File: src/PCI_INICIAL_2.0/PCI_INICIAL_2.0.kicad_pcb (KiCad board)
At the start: 2 copper layers, 60 x 50.8 mm, 9 parts, among them J1 2 male pin header, SW1 Switch, U1 ESP32, U2 MPU9250 Module, U3 TP4056

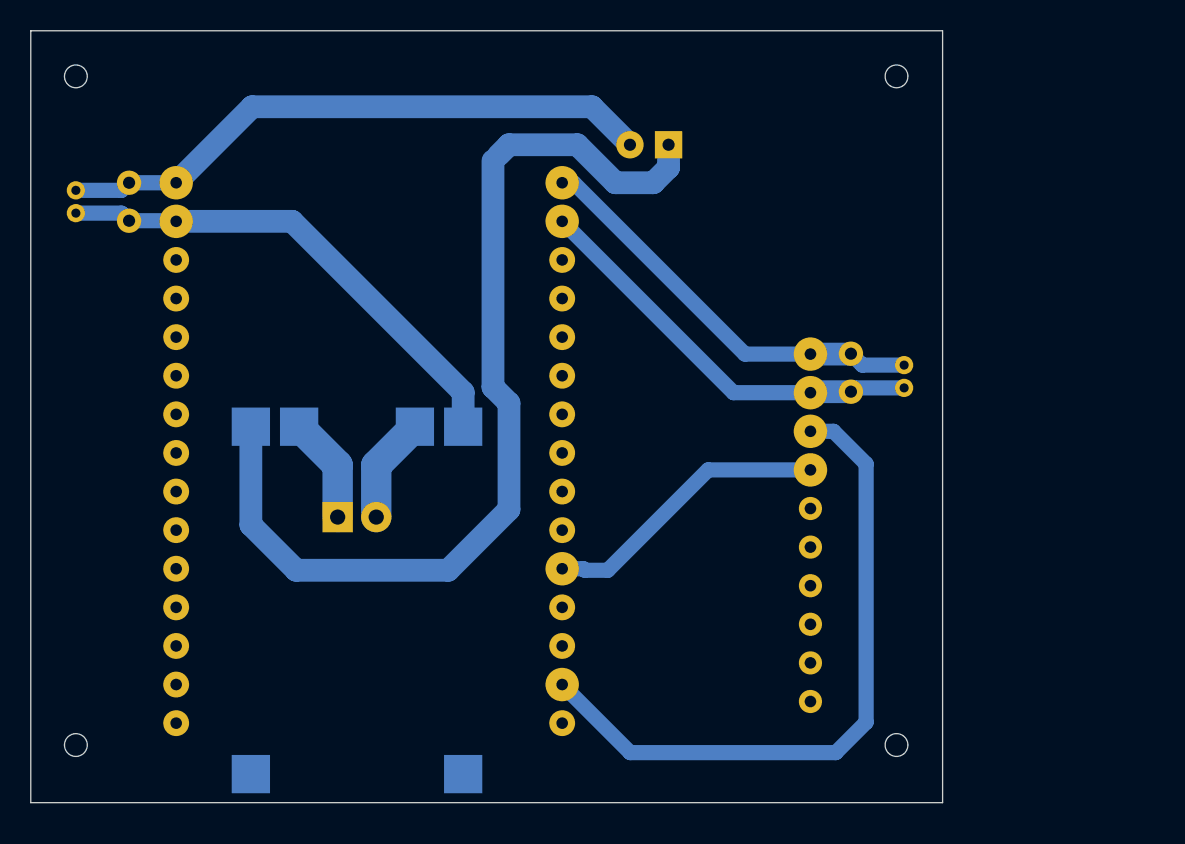
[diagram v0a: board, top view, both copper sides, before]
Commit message: feat: adiciona arquivos 2.0 de PCI
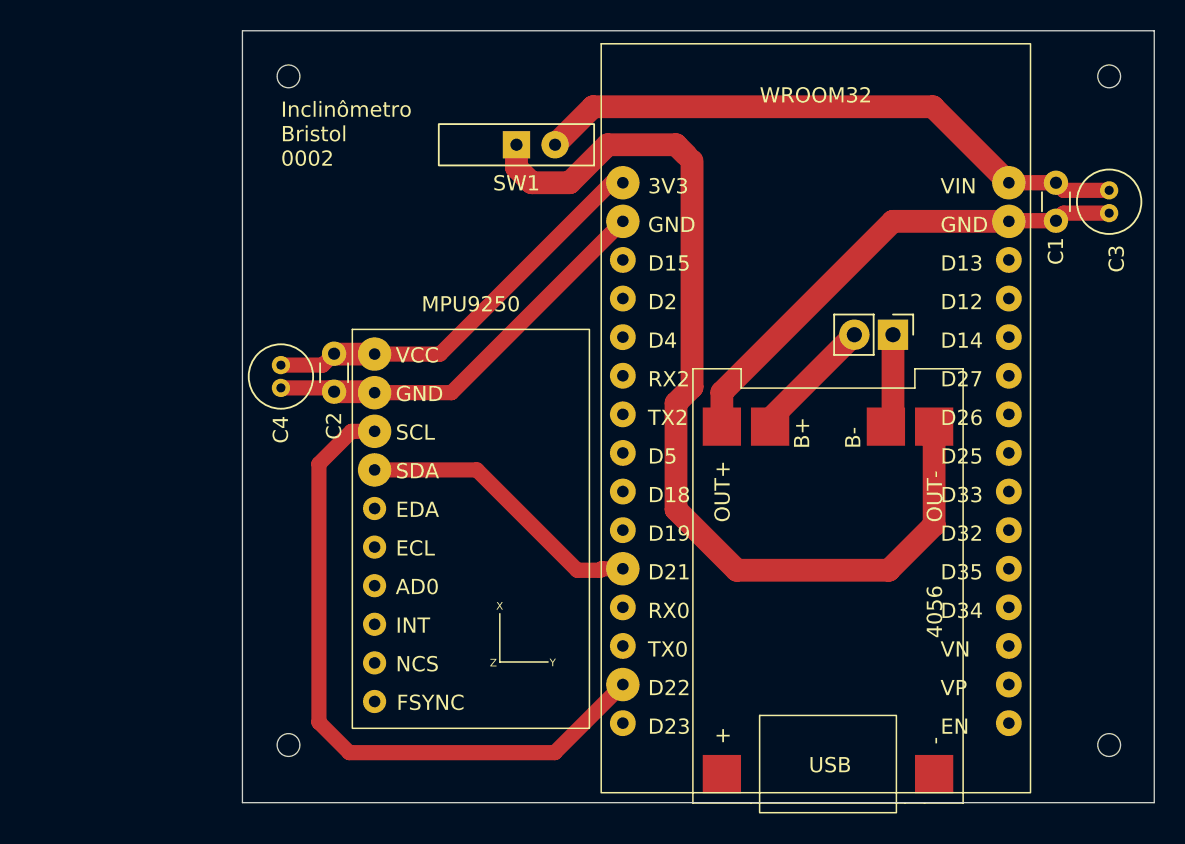
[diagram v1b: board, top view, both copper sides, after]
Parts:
- C1, C2, C3, C4, J1, SW1, U1, U2, U3: moved to F.Cu
- moved C3 68.0 mm to (139.0, 109.5)
- moved C1 61.0 mm to (135.5, 109.0)
- moved C4 41.0 mm to (84.5, 121.0)
- moved J1 38.5 mm to (124.8, 119.0)
- moved C2 34.0 mm to (88.0, 120.2)
- moved U3 31.0 mm to (120.5, 116.7), turned to 0 degrees
- moved U2 16.0 mm to (97.0, 114.5), turned to 0 degrees
- moved SW1 10.0 mm to (100.0, 106.5), turned to 180 degrees
- moved U1 3.99 mm to (107.0, 101.4), turned to 0 degrees
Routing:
- net B+: track 7.00 -> 8.35 mm
- net B-: track 7.00 -> 6.25 mm
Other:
- outline, holes or cut-outs redrawn
